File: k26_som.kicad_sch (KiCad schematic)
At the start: 56 parts, among them J6 PinHeader_1x2_P2.54mm_Drill1.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, M1 XILINX-KRIA-K26, Q19 DTC014T_SOT-416, Q6 PJA3441, Q7 DTC014T_SOT-416

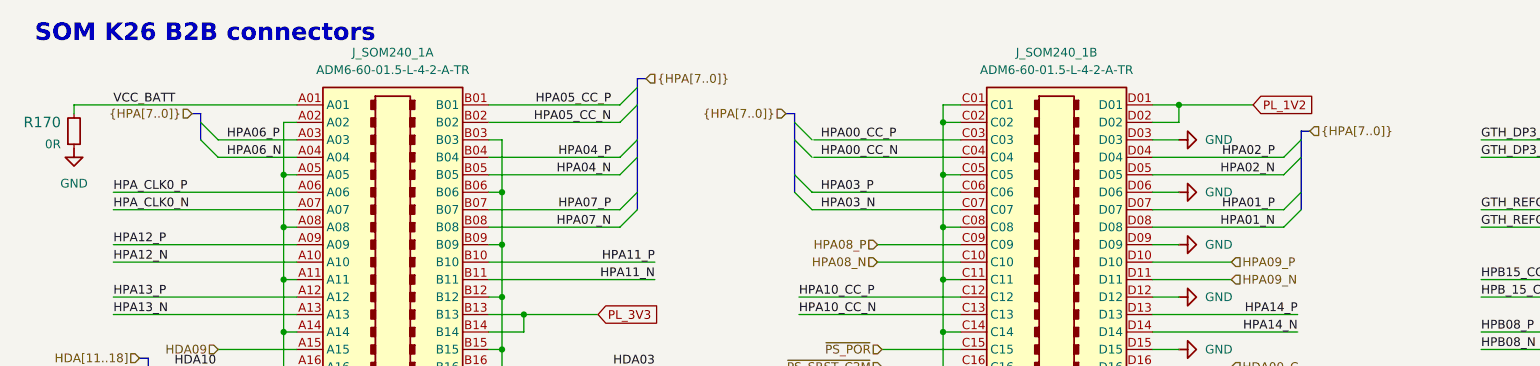
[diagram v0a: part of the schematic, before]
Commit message: Finished first set of LVDS signals
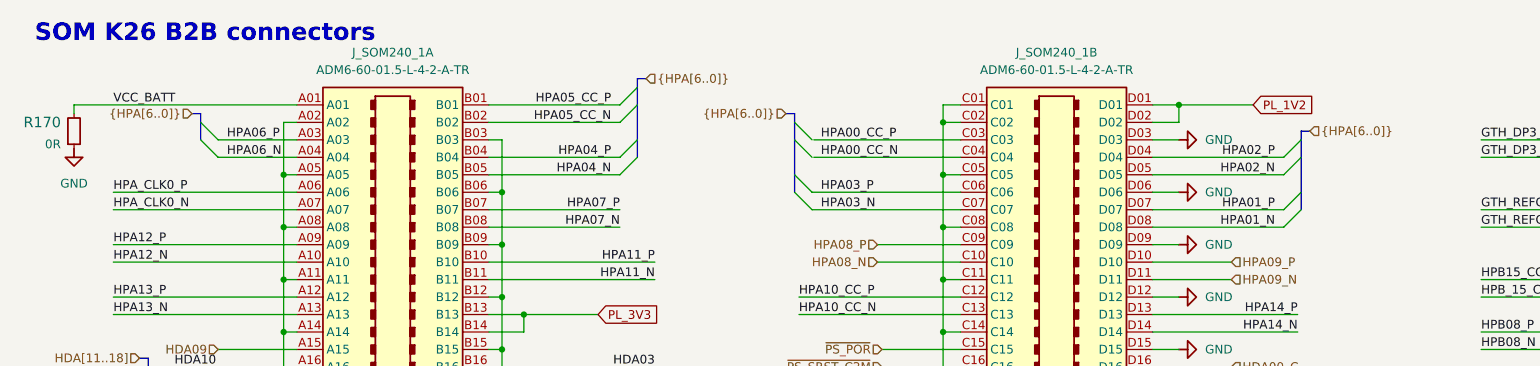
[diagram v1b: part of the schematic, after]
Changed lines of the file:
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@@
 	)
 	(bus_entry
-		(at 101.6 38.1)
-		(size -2.54 2.54)
-		(stroke
-			(width 0)
-			(type default)
-		)
-	)
-	(bus_entry
 		(at 194.31 134.62)
 		(size 2.54 -2.54)
@@
 	)
 	(bus_entry
-		(at 99.06 43.18)
-		(size 2.54 -2.54)
-		(stroke
-			(width 0)
-			(type default)
-		)
-	)
-	(bus_entry
 		(at 129.54 101.6)
 		(size -2.54 -2.54)
@@
 		)
 	)
-	(bus
-		(pts
-			(xy 101.6 30.48) (xy 101.6 33.02)
-		)
-		(stroke
-			(width 0)
-			(type default)
-		)
-	)
 	(wire
 		(pts
@@
 		)
 	)
+	(bus
+		(pts
+			(xy 101.6 30.48) (xy 101.6 33.02)
+		)
+		(stroke
+			(width 0)
+			(type default)
+		)
+	)
 	(wire
 		(pts
@@
 		)
 	)
-	(bus
-		(pts
-			(xy 101.6 38.1) (xy 101.6 40.64)
-		)
-		(stroke
-			(width 0)
-			(type default)
-		)
-	)
 	(wire
 		(pts
@@
 		)
 	)
-	(bus
-		(pts
-			(xy 101.6 33.02) (xy 101.6 38.1)
-		)
-		(stroke
-			(width 0)
-			(type default)
-		)
-	)
 	(wire
 		(pts
@@
 	)
 	(label "HPA07_N"
-		(at 97.79 43.18 180)
+		(at 99.06 43.18 180)
 		(effects
 			(font
@@
 	)
 	(label "HPA07_P"
-		(at 97.79 40.64 180)
+		(at 99.06 40.64 180)
 		(effects
 			(font
@@
 		)
 	)
-	(hierarchical_label "{HPA[7..0]}"
+	(hierarchical_label "{HPA[6..0]}"
 		(shape input)
 		(at 102.87 21.59 0)
@@
 		)
 	)
-	(hierarchical_label "{HPA[7..0]}"
+	(hierarchical_label "{HPA[6..0]}"
 		(shape input)
 		(at 199.39 29.21 0)
@@
 		)
 	)
-	(hierarchical_label "{HPA[7..0]}"
+	(hierarchical_label "{HPA[6..0]}"
 		(shape input)
 		(at 123.19 26.67 180)
@@
 		)
 	)
-	(hierarchical_label "{HPA[7..0]}"
+	(hierarchical_label "{HPA[6..0]}"
 		(shape input)
 		(at 36.83 26.67 180)

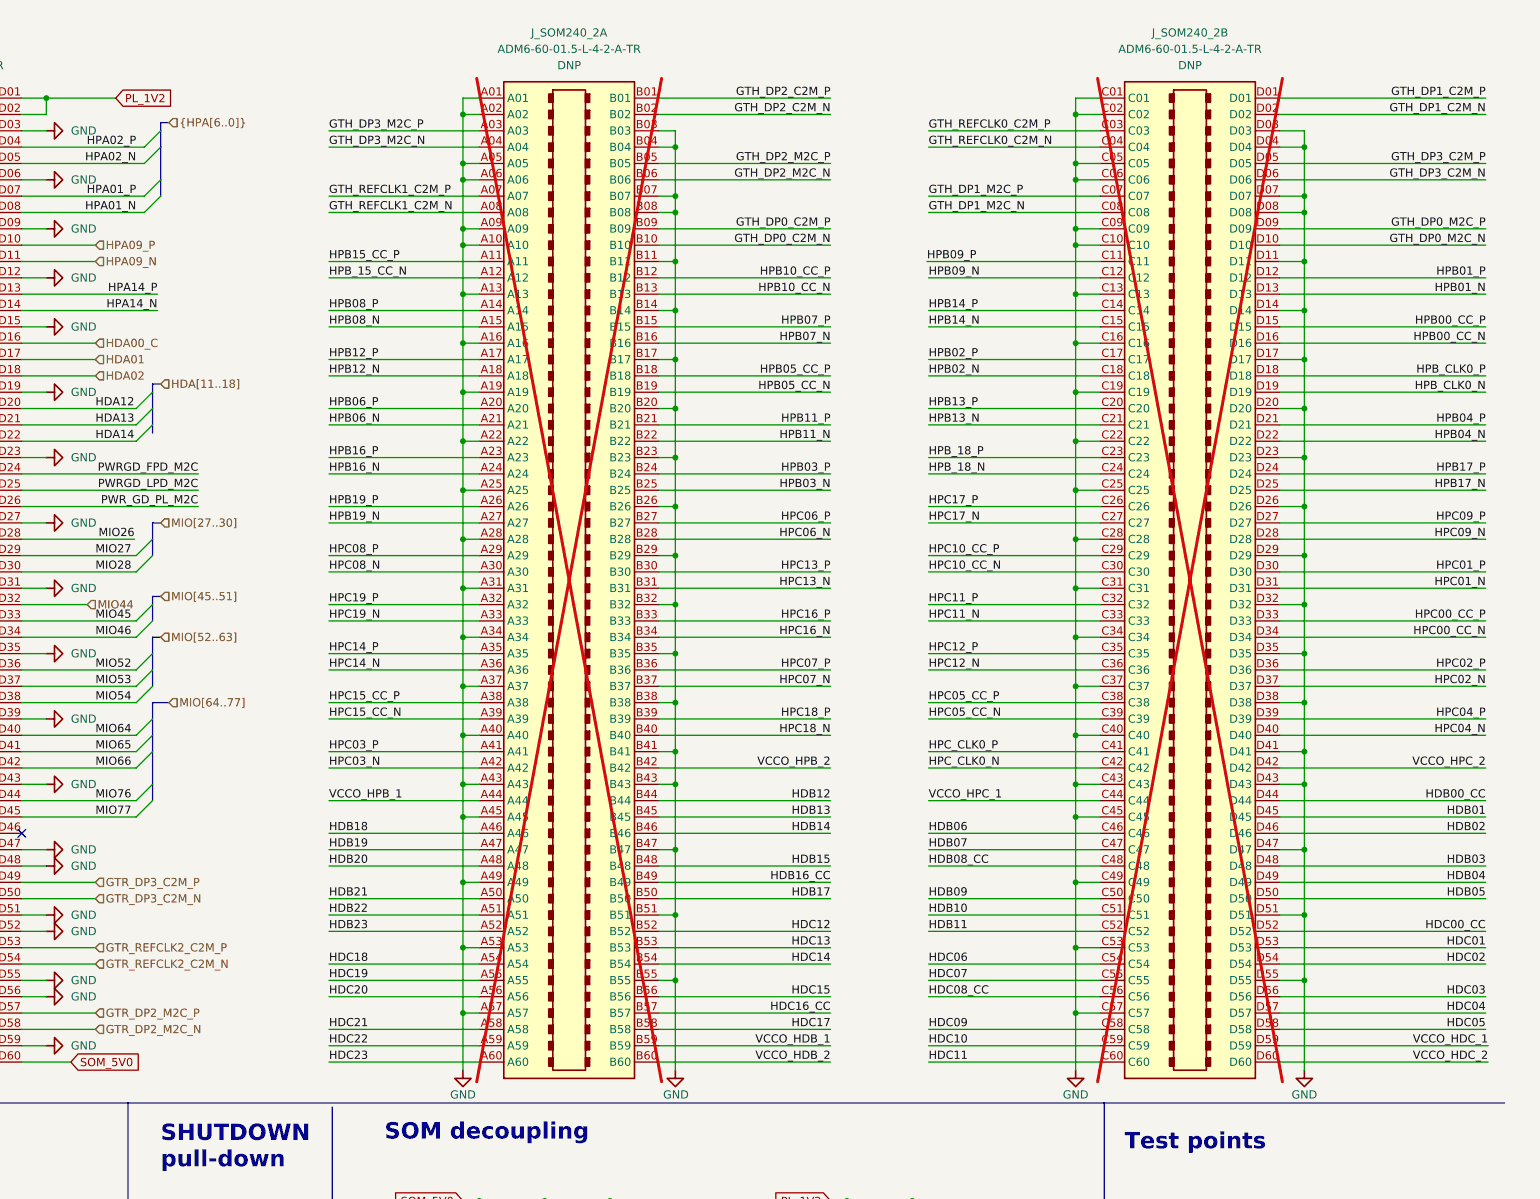
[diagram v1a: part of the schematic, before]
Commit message: Added second radar board connector, but haven't routed LVDS lines yet
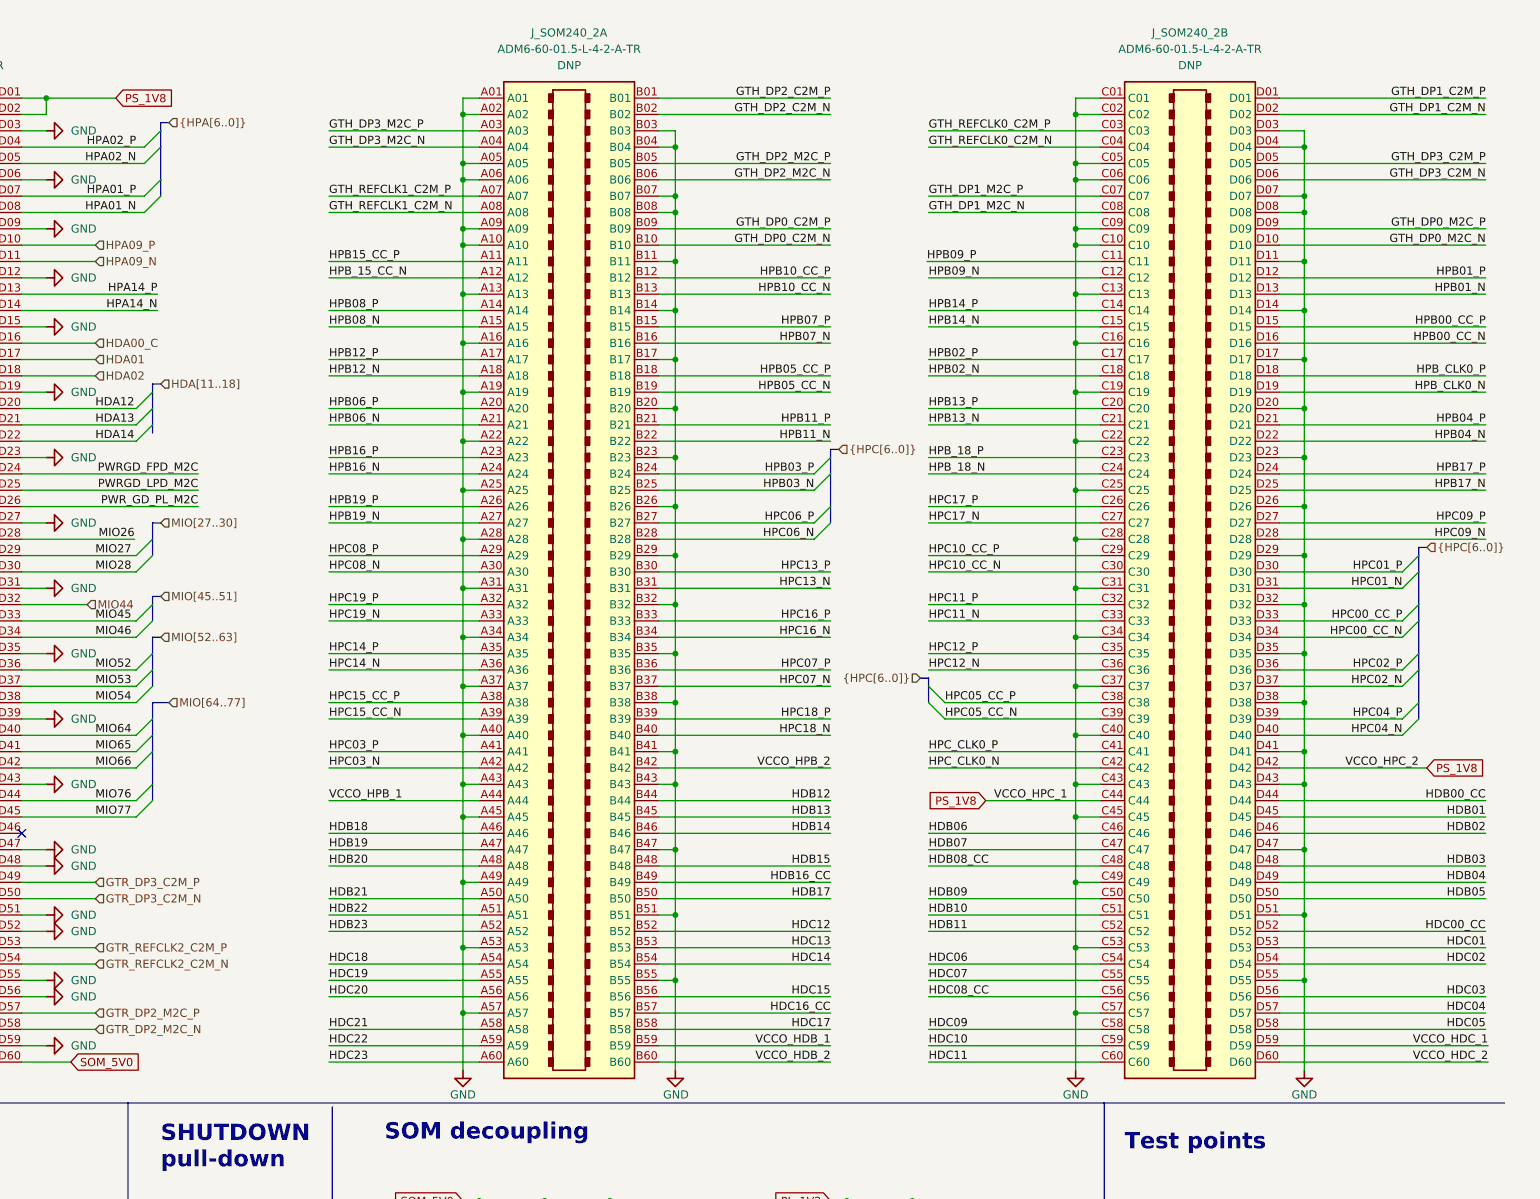
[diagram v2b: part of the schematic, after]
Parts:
- J_SOM240_2: now fitted
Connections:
- net VCCO_HPC_2 is gone; now on net PS_1V8: J_SOM240_2.D42
- net PL_1V2: no longer J_SOM240_1.D01, J_SOM240_1.D02
- net VCCO_HPC_1 renamed PS_1V8
- net PS_1V8: now also J_SOM240_1.D01, J_SOM240_1.D02

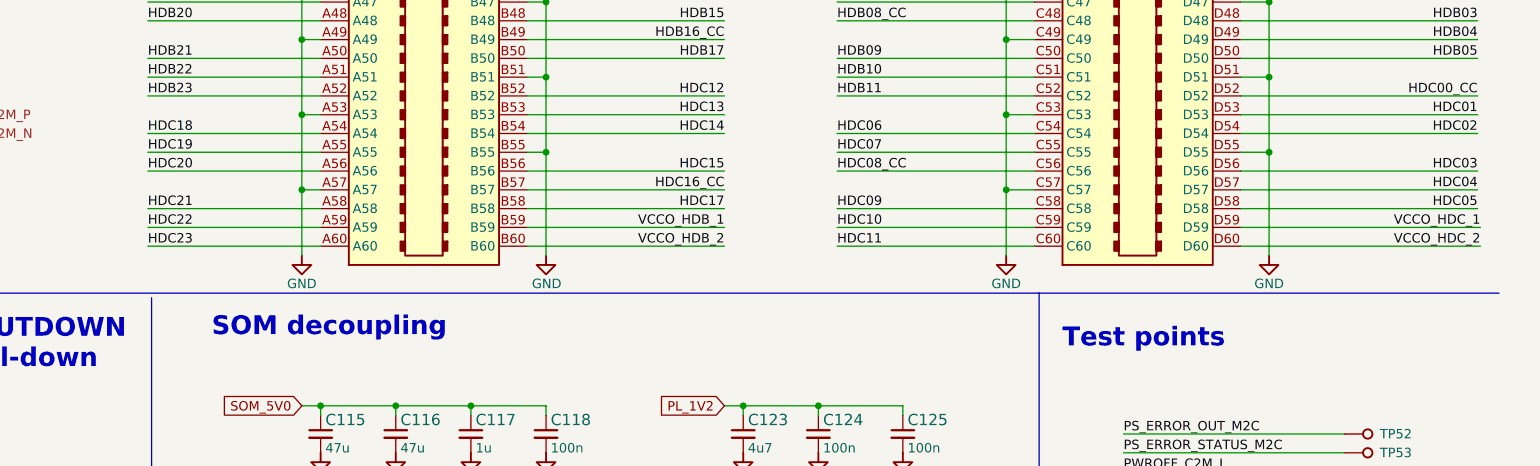
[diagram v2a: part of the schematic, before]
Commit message: Added second CAN interface, but haven't routed yet
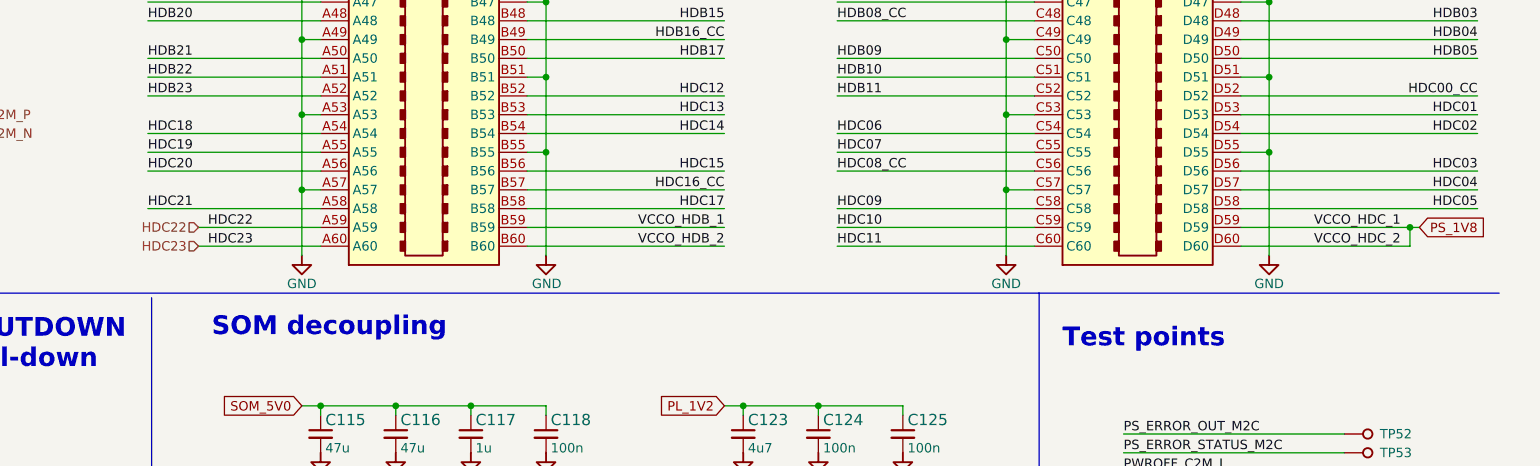
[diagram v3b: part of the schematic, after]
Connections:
- net VCCO_HDC_1 is gone; now on net PS_1V8: J_SOM240_2.D59
- net VCCO_HDC_2 is gone; now on net PS_1V8: J_SOM240_2.D60
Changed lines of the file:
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@@
 	)
 	(junction
+		(at 394.97 172.72)
+		(diameter 0)
+		(color 0 0 0 0)
+	)
+	(junction
 		(at 278.13 33.02)
 		(diameter 0)
@@
 	(wire
 		(pts
+			(xy 231.14 172.72) (xy 247.65 172.72)
+		)
+		(stroke
+			(width 0)
+			(type default)
+		)
+	)
+	(wire
+		(pts
 			(xy 372.11 50.8) (xy 375.92 50.8)
 		)
@@
 	(wire
 		(pts
-			(xy 224.282 172.72) (xy 247.65 172.72)
-		)
-		(stroke
-			(width 0)
-			(type default)
-		)
-	)
-	(wire
-		(pts
 			(xy 372.11 121.92) (xy 391.16 121.92)
 		)
@@
 	(wire
 		(pts
-			(xy 372.11 175.26) (xy 404.495 175.26)
+			(xy 372.11 175.26) (xy 394.97 175.26)
 		)
 		(stroke
@@
 	(wire
 		(pts
-			(xy 224.282 175.26) (xy 247.65 175.26)
+			(xy 231.14 175.26) (xy 247.65 175.26)
 		)
 		(stroke
@@
 	(wire
 		(pts
+			(xy 394.97 172.72) (xy 394.97 175.26)
+		)
+		(stroke
+			(width 0)
+			(type default)
+		)
+	)
+	(wire
+		(pts
 			(xy 317.5 142.24) (xy 344.17 142.24)
 		)
@@
 	(wire
 		(pts
-			(xy 372.11 172.72) (xy 404.495 172.72)
+			(xy 372.11 172.72) (xy 394.97 172.72)
 		)
 		(stroke
@@
 		)
 	)
+	(wire
+		(pts
+			(xy 394.97 172.72) (xy 396.24 172.72)
+		)
+		(stroke
+			(width 0)
+			(type default)
+		)
+	)
 	(polyline
 		(pts
@@
 	)
 	(label "HDC23"
-		(at 224.282 175.26 0)
+		(at 232.41 175.26 0)
 		(effects
 			(font
@@
 	)
 	(label "VCCO_HDC_1"
-		(at 404.495 172.72 180)
+		(at 393.7 172.72 180)
 		(effects
 			(font
@@
 	)
 	(label "VCCO_HDC_2"
-		(at 404.495 175.26 180)
+		(at 393.7 175.26 180)
 		(effects
 			(font
@@
 	)
 	(label "HDC22"
-		(at 224.282 172.72 0)
+		(at 232.41 172.72 0)
 		(effects
 			(font
@@
 		)
 	)
+	(global_label "PS_1V8"
+		(shape input)
+		(at 396.24 172.72 0)
+		(fields_autoplaced yes)
+		(effects
+			(font
+				(size 1.27 1.27)
+			)
+			(justify left)
+		)
+		(property "Intersheetrefs" "${INTERSHEET_REFS}"
+			(at 405.5257 172.72 0)
+			(effects
+				(font
+					(size 1.27 1.27)
+				)
+				(justify left)
+				(hide yes)
+			)
+		)
+	)
 	(global_label "USB_5V"
 		(shape input)
@@
 		)
 	)
+	(hierarchical_label "HDC22"
+		(shape input)
+		(at 231.14 172.72 180)
+		(effects
+			(font
+				(size 1.27 1.27)
+			)
+			(justify right)
+		)
+	)
 	(hierarchical_label "HDA01"
 		(shape input)
@@
 		)
 	)
+	(hierarchical_label "HDC23"
+		(shape input)
+		(at 231.14 175.26 180)
+		(effects
+			(font
+				(size 1.27 1.27)
+			)
+			(justify right)
+		)
+	)
